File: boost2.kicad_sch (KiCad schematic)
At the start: 28 parts, among them Q7 BSC059N04LS6, Q8 BSC059N04LS6, U8 TPS43061

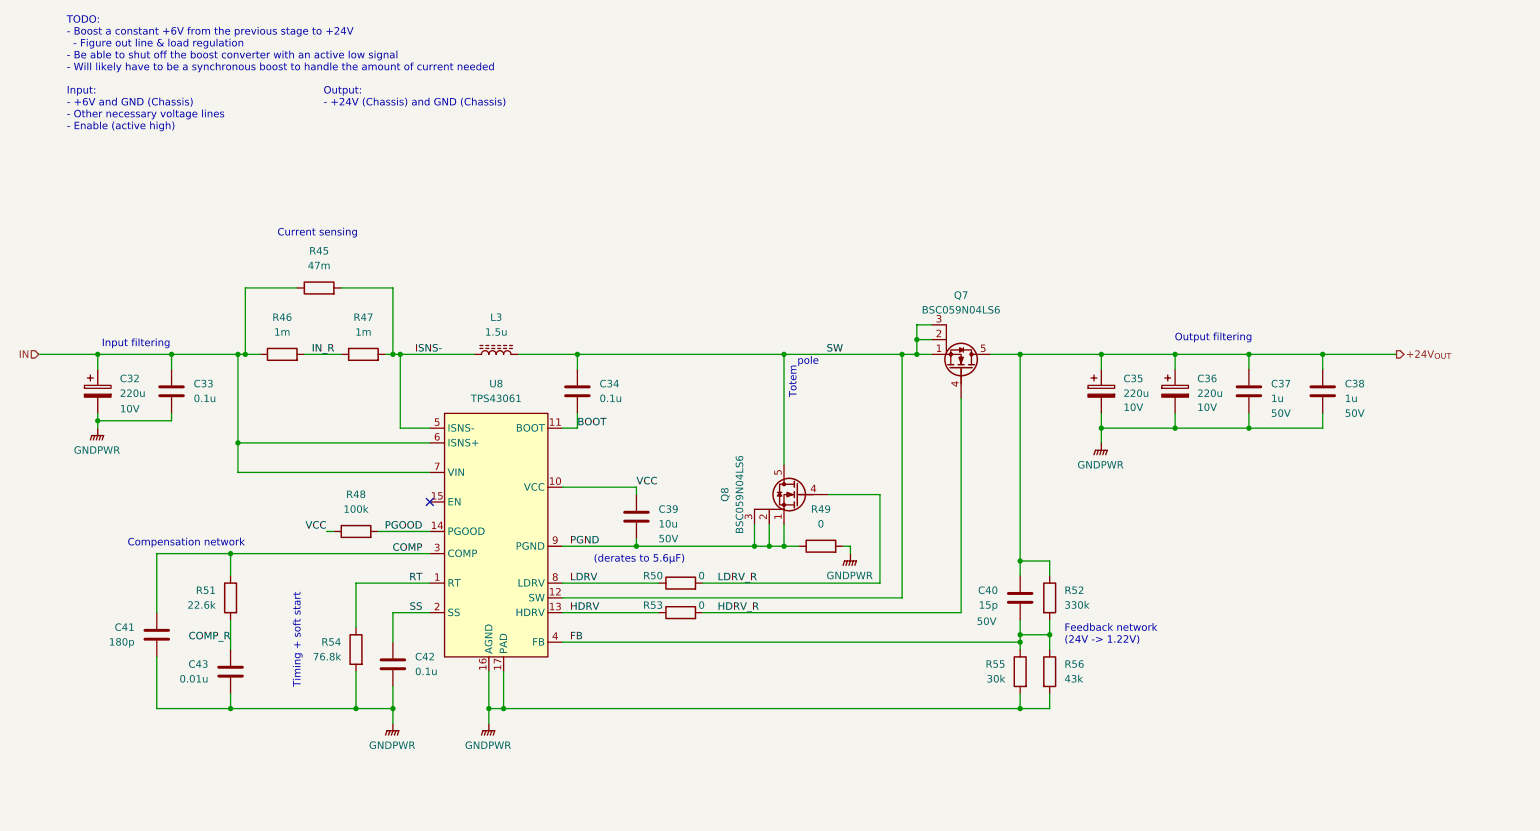
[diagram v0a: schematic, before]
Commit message: Specc'd all components + started creating rev 1b boards
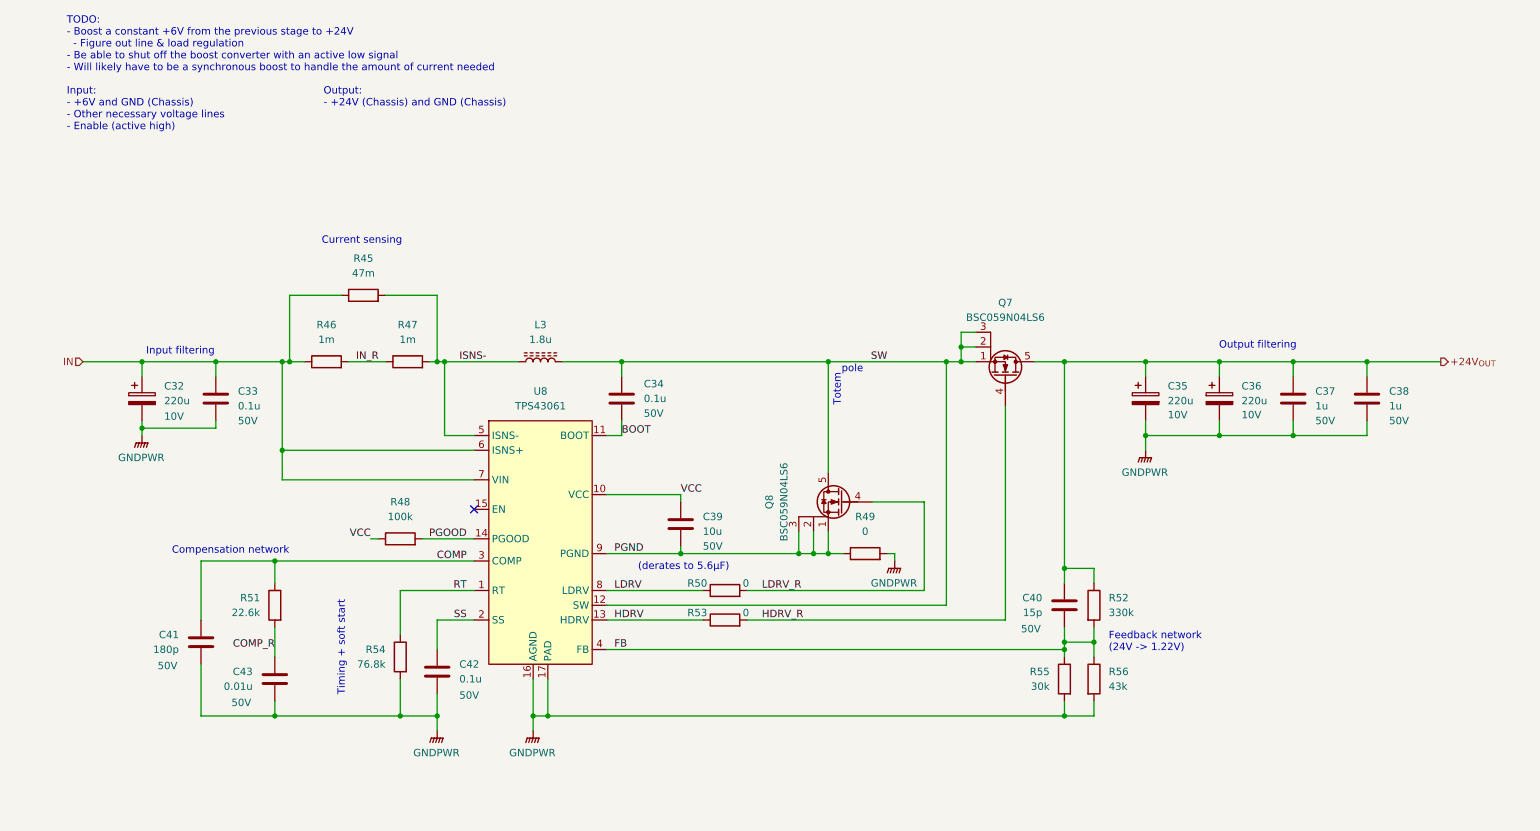
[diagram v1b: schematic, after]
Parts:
- C33, C34, C42: Mouser Part Number (none) -> 581-KGM15BR71H104JT; Voltage Rating (none) -> 50V
- C41: Mouser Part Number (none) -> 603-CC603JPNPO9BN181; Voltage Rating (none) -> 50V
- C43: Mouser Part Number (none) -> 187-CL10B103KC8NNNC; Voltage Rating (none) -> 50V
- L3: value 1.5u -> 1.8u
- R48: Mouser Part Number (none) -> 660-RN73H1JTD1003D25
- R49, R50, R53: Mouser Part Number (none) -> 660-RK73Z1JTTDD
- R51: Mouser Part Number (none) -> 603-RC0603FR-0722K6L
- R52: Mouser Part Number (none) -> 603-RT0603DRD07330KL
- R54: Mouser Part Number (none) -> 660-RN73H1JTD7682B25
- R55: Mouser Part Number (none) -> 660-RN73H1JTD3002B50
- R56: Mouser Part Number (none) -> 603-RT0603DRD0743KL
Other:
- moved on the sheet: C32, C33, C34, C35, C36, C37, C38, C39, C40, C41, C42, C43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

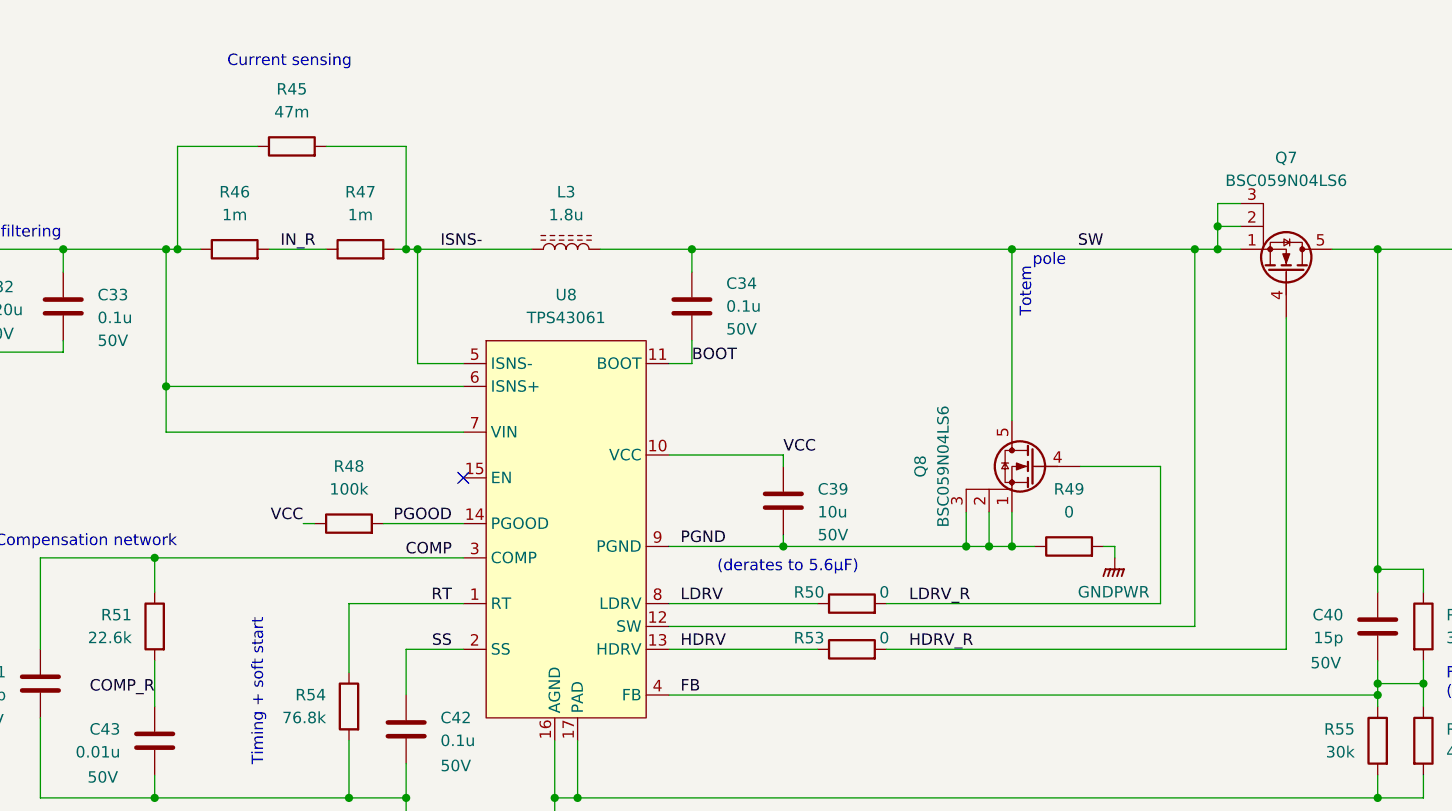
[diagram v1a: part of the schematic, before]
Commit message: Add test points to all subsheets
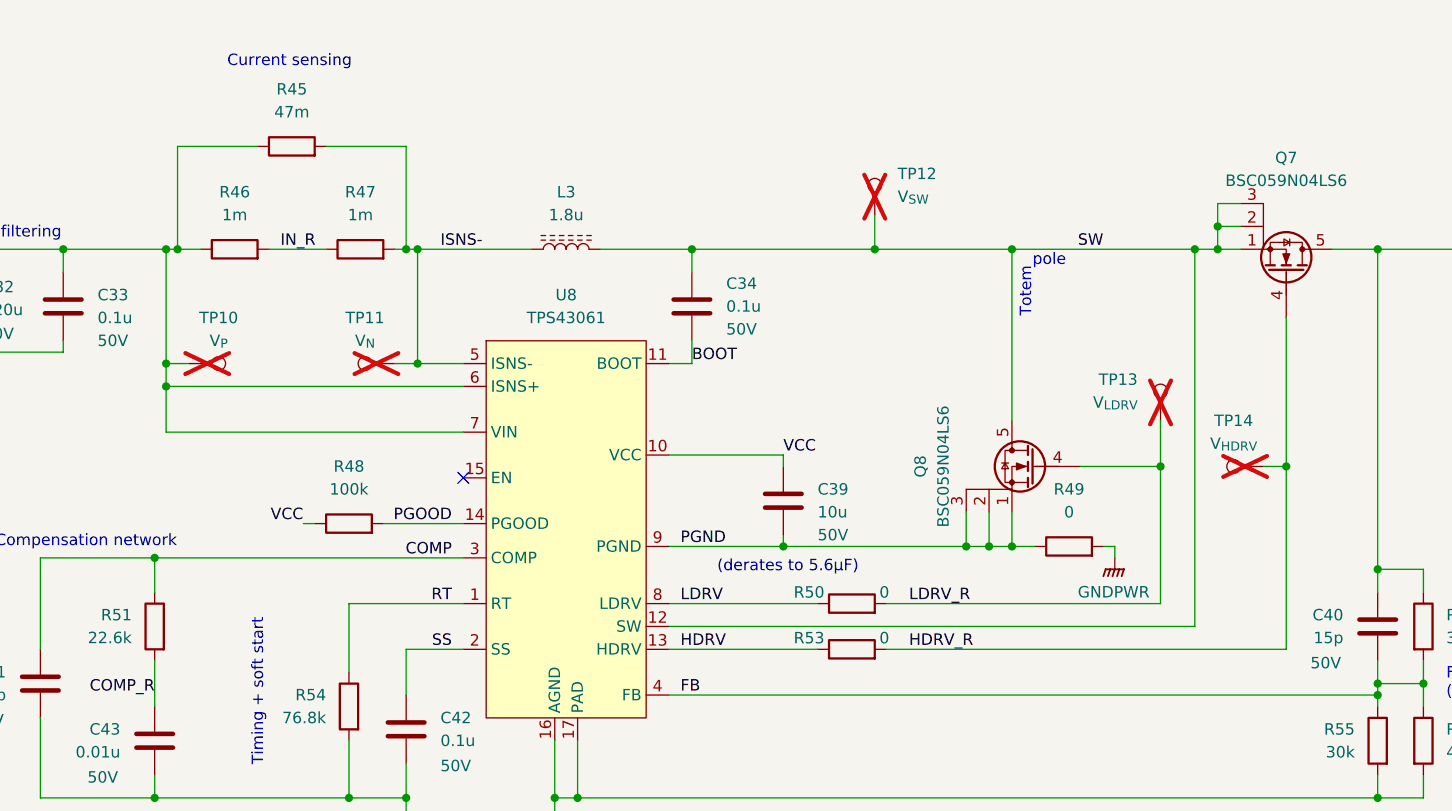
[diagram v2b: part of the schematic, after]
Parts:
- added TP10: V_{P}, TestPoint:TestPoint_Bridge_Pitch2.0mm_Drill0.7mm, symbol Connector:TestPoint
- added TP11: V_{N}, TestPoint:TestPoint_Bridge_Pitch2.0mm_Drill0.7mm, symbol Connector:TestPoint
- added TP12: V_{SW}, TestPoint:TestPoint_Bridge_Pitch2.0mm_Drill0.7mm, symbol Connector:TestPoint
- added TP13: V_{LDRV}, TestPoint:TestPoint_Bridge_Pitch2.0mm_Drill0.7mm, symbol Connector:TestPoint
- added TP14: V_{HDRV}, TestPoint:TestPoint_Bridge_Pitch2.0mm_Drill0.7mm, symbol Connector:TestPoint
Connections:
- net HDRV_R: now also TP14.1
- net IN: now also TP10.1
- net ISNS-: now also TP11.1
- net LDRV_R: now also TP13.1
- net SW: now also TP12.1

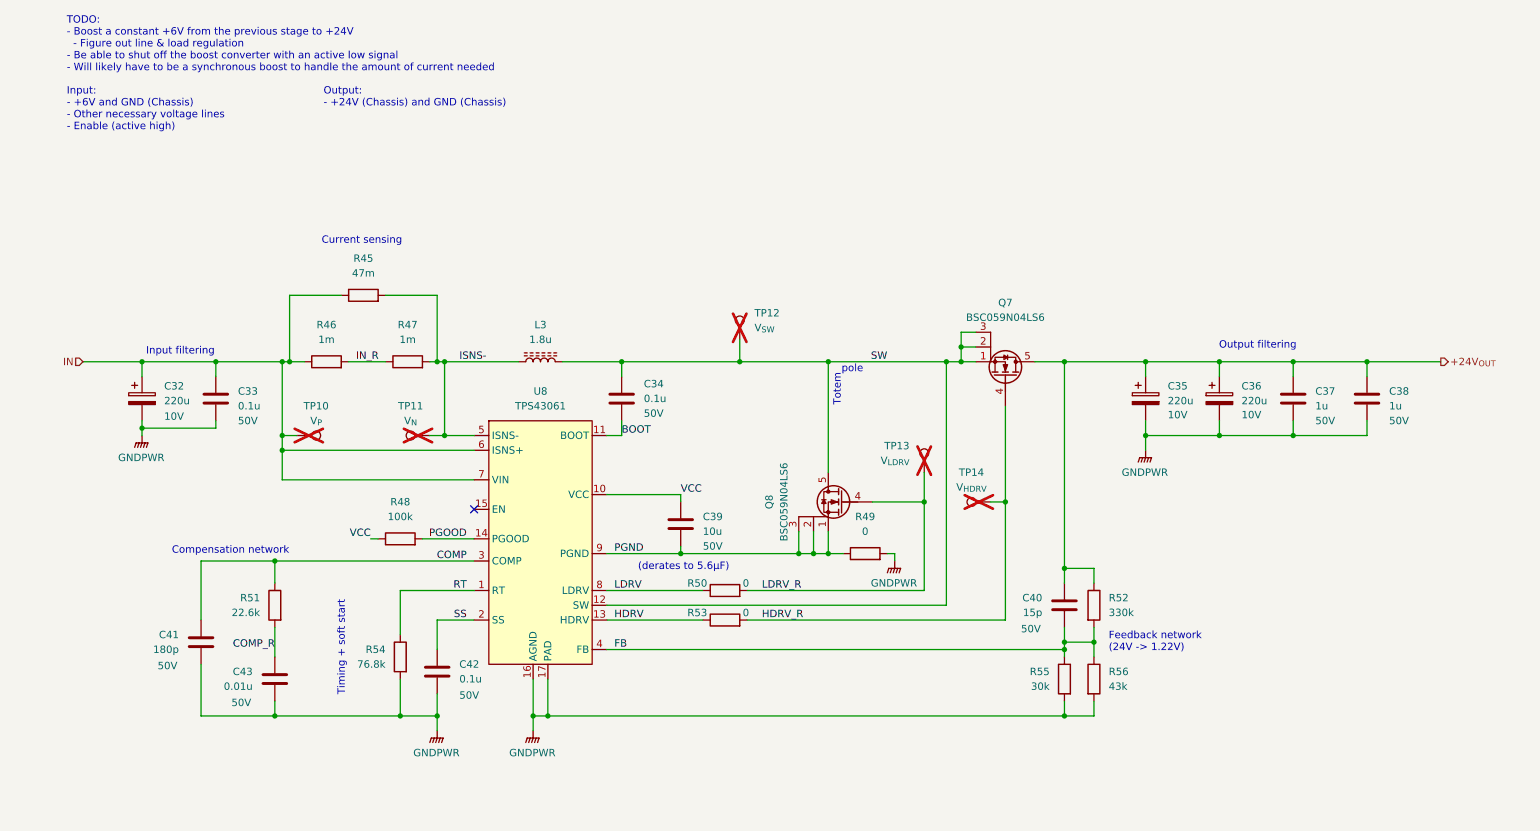
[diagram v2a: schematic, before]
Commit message: Renumbered components for rev 1b layout
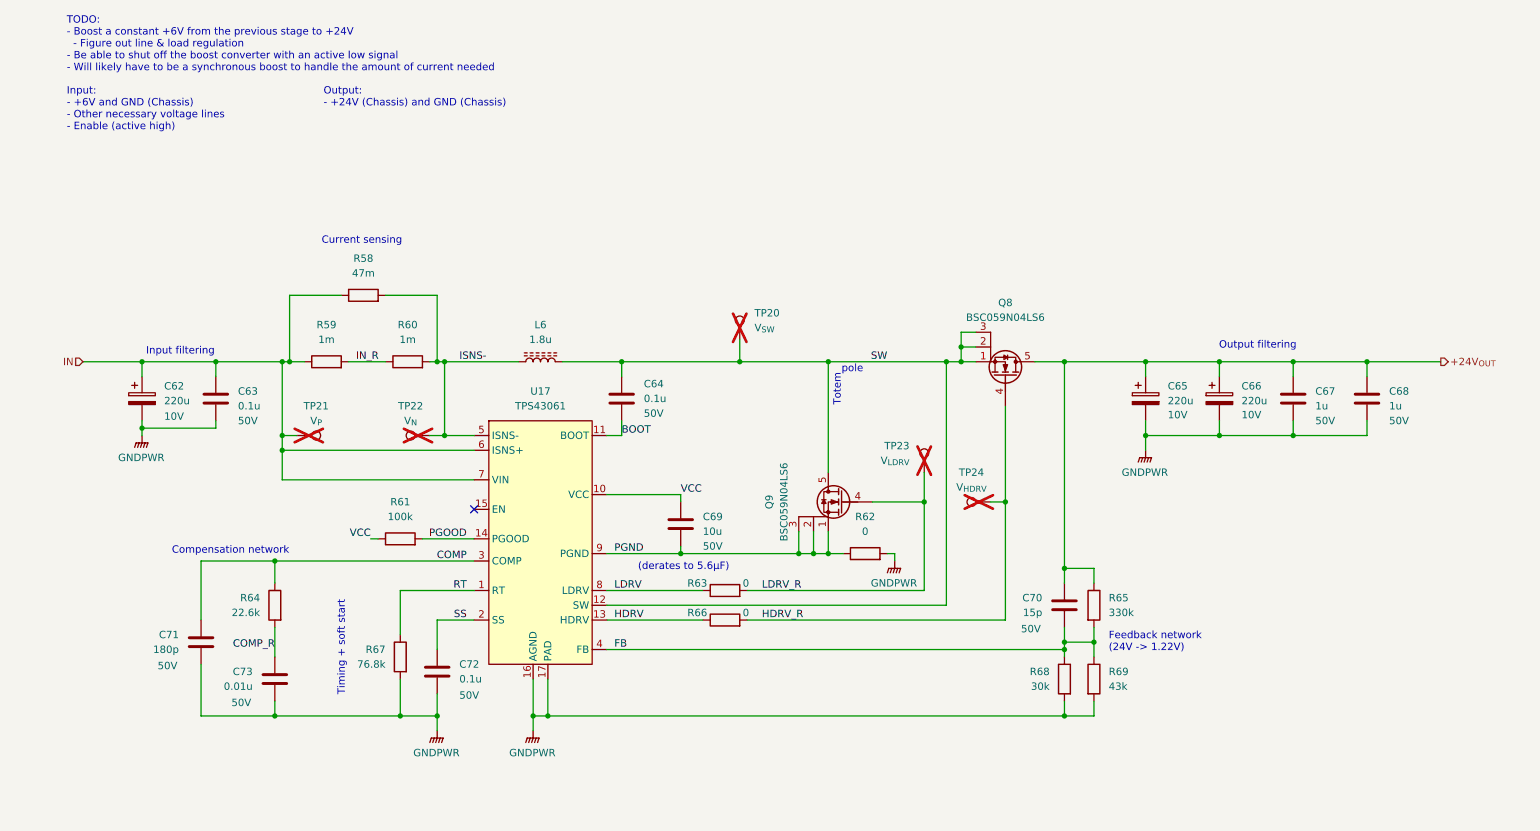
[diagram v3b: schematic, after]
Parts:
- renumbered C32 to C62, C33 to C63, C34 to C64, C35 to C65, C36 to C66, C37 to C67, C38 to C68, C39 to C69, C40 to C70, C41 to C71, C42 to C72, C43 to C73, L3 to L6, Q7 to Q8, Q8 to Q9, R45 to R58, R46 to R59, R47 to R60, R48 to R61, R49 to R62, R50 to R63, R51 to R64, R52 to R65, R53 to R66, R54 to R67, R55 to R68, R56 to R69, TP12 to TP20, TP10 to TP21, TP11 to TP22, TP13 to TP23, TP14 to TP24, U8 to U17
